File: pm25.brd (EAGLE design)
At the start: 47 x 33 mm, 12 parts, among them U2 CCS811B-JOPD500, U4 SI7021-A20-GM1R

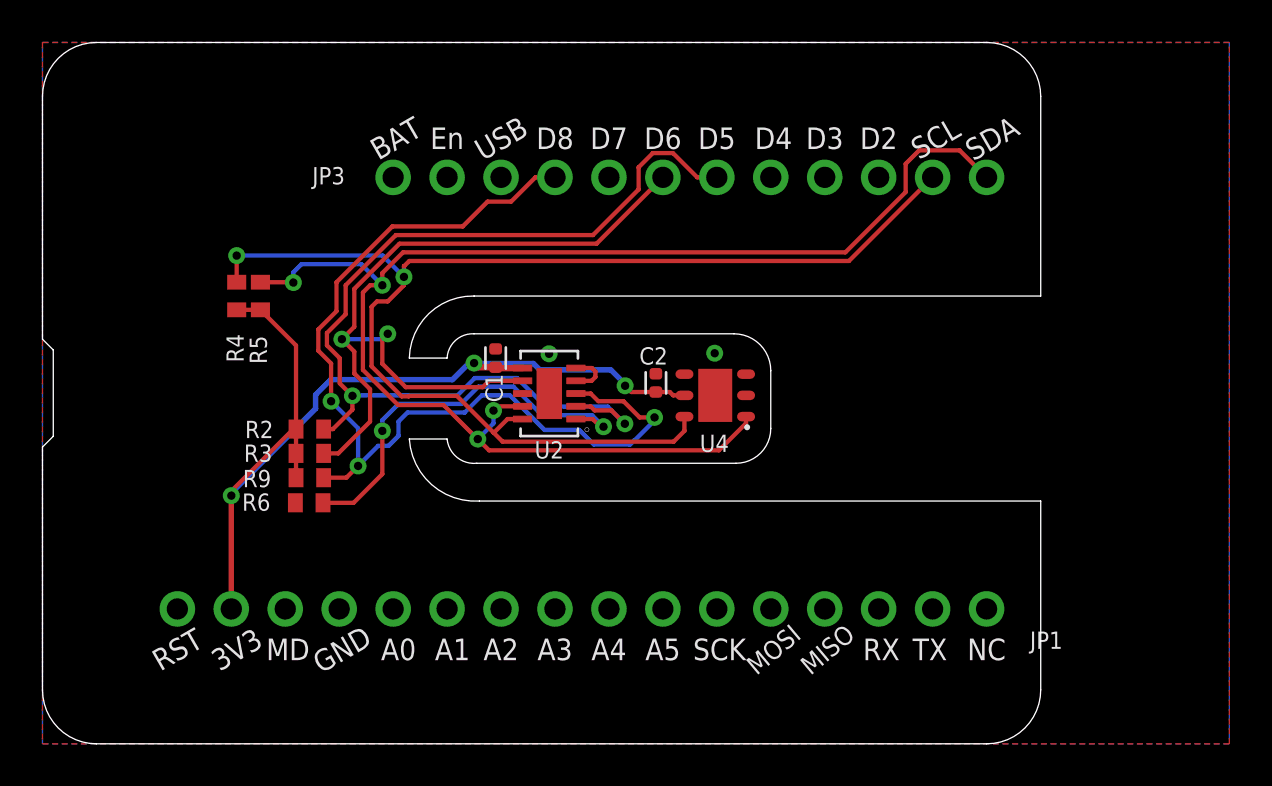
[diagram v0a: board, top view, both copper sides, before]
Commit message: Shrink width to 0.9" standard
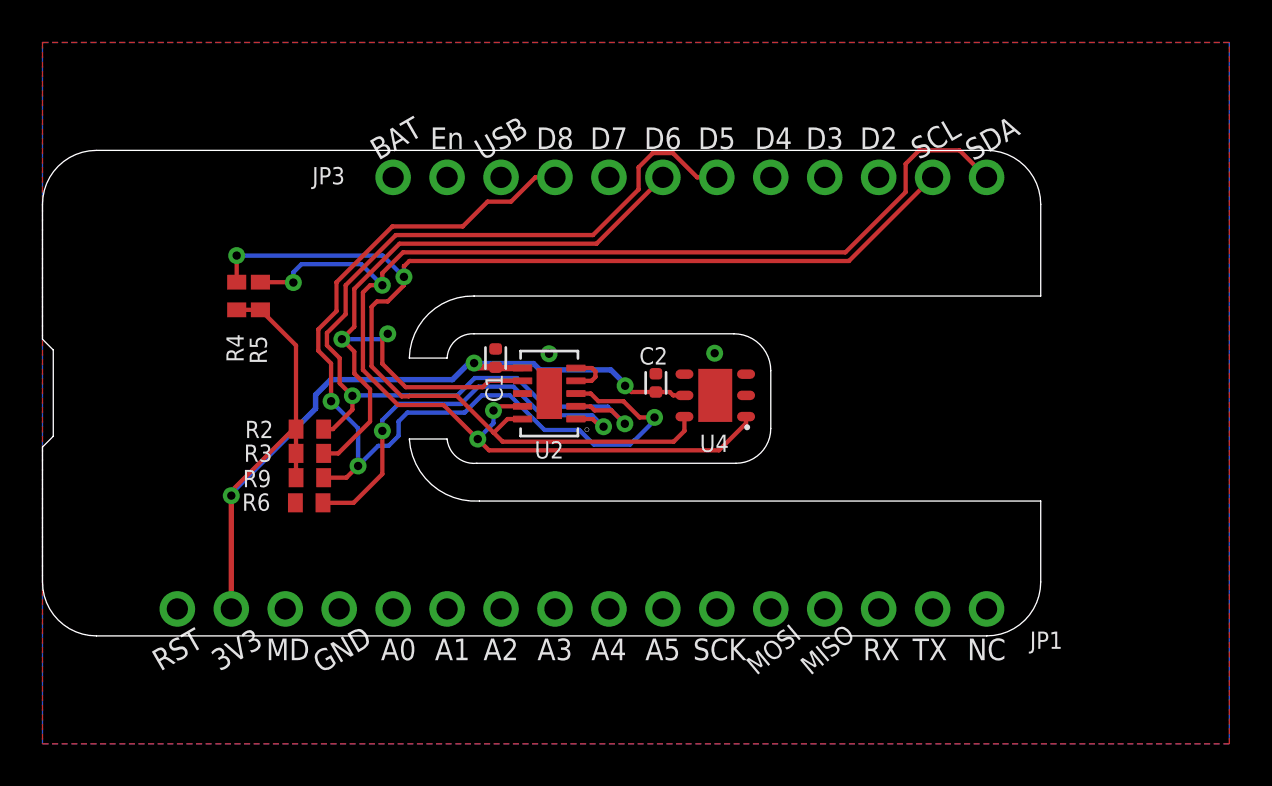
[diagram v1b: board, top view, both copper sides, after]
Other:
- board size 47 x 33 mm -> 47 x 22.9 mm
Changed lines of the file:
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@@
 <setting verticaltext="up"/>
 </settings>
-<grid distance="5" unitdist="mil" unit="mm" style="lines" multiple="1" display="no" altdistance="0.025" altunitdist="inch" altunit="mil"/>
+<grid distance="5" unitdist="mil" unit="inch" style="lines" multiple="1" display="no" altdistance="0.025" altunitdist="inch" altunit="mil"/>
 <layers>
-<layer number="1" name="Top" color="4" fill="1" visible="yes" active="yes"/>
+<layer number="1" name="Top" color="4" fill="1" visible="no" active="yes"/>
 <layer number="2" name="Route2" color="1" fill="3" visible="no" active="no"/>
 <layer number="3" name="Route3" color="4" fill="3" visible="no" active="no"/>
@@
 <layer number="14" name="Route14" color="1" fill="6" visible="no" active="no"/>
 <layer number="15" name="Route15" color="4" fill="6" visible="no" active="no"/>
-<layer number="16" name="Bottom" color="1" fill="1" visible="yes" active="yes"/>
-<layer number="17" name="Pads" color="2" fill="1" visible="yes" active="yes"/>
-<layer number="18" name="Vias" color="2" fill="1" visible="yes" active="yes"/>
-<layer number="19" name="Unrouted" color="6" fill="1" visible="yes" active="yes"/>
+<layer number="16" name="Bottom" color="1" fill="1" visible="no" active="yes"/>
+<layer number="17" name="Pads" color="2" fill="1" visible="no" active="yes"/>
+<layer number="18" name="Vias" color="2" fill="1" visible="no" active="yes"/>
+<layer number="19" name="Unrouted" color="6" fill="1" visible="no" active="yes"/>
 <layer number="20" name="Dimension" color="15" fill="1" visible="yes" active="yes"/>
-<layer number="21" name="tPlace" color="14" fill="1" visible="yes" active="yes"/>
-<layer number="22" name="bPlace" color="14" fill="1" visible="yes" active="yes"/>
-<layer number="23" name="tOrigins" color="14" fill="1" visible="yes" active="yes"/>
-<layer number="24" name="bOrigins" color="13" fill="1" visible="yes" active="yes"/>
-<layer number="25" name="tNames" color="7" fill="1" visible="yes" active="yes"/>
-<layer number="26" name="bNames" color="7" fill="1" visible="yes" active="yes"/>
+<layer number="21" name="tPlace" color="14" fill="1" visible="no" active="yes"/>
+<layer number="22" name="bPlace" color="14" fill="1" visible="no" active="yes"/>
+<layer number="23" name="tOrigins" color="14" fill="1" visible="no" active="yes"/>
+<layer number="24" name="bOrigins" color="13" fill="1" visible="no" active="yes"/>
+<layer number="25" name="tNames" color="7" fill="1" visible="no" active="yes"/>
+<layer number="26" name="bNames" color="7" fill="1" visible="no" active="yes"/>
 <layer number="27" name="tValues" color="7" fill="1" visible="no" active="yes"/>
 <layer number="28" name="bValues" color="7" fill="1" visible="no" active="yes"/>
@@
 <layer number="37" name="tTest" color="7" fill="1" visible="no" active="yes"/>
 <layer number="38" name="bTest" color="7" fill="1" visible="no" active="yes"/>
-<layer number="39" name="tKeepout" color="4" fill="11" visible="yes" active="yes"/>
-<layer number="40" name="bKeepout" color="1" fill="11" visible="yes" active="yes"/>
-<layer number="41" name="tRestrict" color="4" fill="10" visible="yes" active="yes"/>
-<layer number="42" name="bRestrict" color="1" fill="10" visible="yes" active="yes"/>
+<layer number="39" name="tKeepout" color="4" fill="11" visible="no" active="yes"/>
+<layer number="40" name="bKeepout" color="1" fill="11" visible="no" active="yes"/>
+<layer number="41" name="tRestrict" color="4" fill="10" visible="no" active="yes"/>
+<layer number="42" name="bRestrict" color="1" fill="10" visible="no" active="yes"/>
 <layer number="43" name="vRestrict" color="2" fill="10" visible="no" active="yes"/>
 <layer number="44" name="Drills" color="7" fill="1" visible="no" active="yes"/>
@@
 <layer number="49" name="Reference" color="7" fill="1" visible="no" active="yes"/>
 <layer number="50" name="dxf" color="7" fill="1" visible="no" active="no"/>
-<layer number="51" name="tDocu" color="7" fill="1" visible="yes" active="yes"/>
-<layer number="52" name="bDocu" color="7" fill="1" visible="yes" active="yes"/>
+<layer number="51" name="tDocu" color="7" fill="1" visible="no" active="yes"/>
+<layer number="52" name="bDocu" color="7" fill="1" visible="no" active="yes"/>
 <layer number="53" name="tGND_GNDA" color="7" fill="9" visible="no" active="no"/>
 <layer number="54" name="bGND_GNDA" color="1" fill="9" visible="no" active="no"/>
@@
 <fusionsync huburn="a.cGVyc29uYWw6dWUyZDcxOWFm" projecturn="a.cGVyc29uYWw6dWUyZDcxOWFmIzIwMTkwMzIxMTgzNjY2NTgx" f3durn="urn:adsk.wipprod:dm.lineage:of-WC7iUTR6j-QJaXZ4WSA" pcbguid="2ada34ed-02e3-4764-ae65-c304e2d58fe2" lastpulledtime="" lastsyncedchangeguid="c324f360-4e1b-41e3-ea26-84c460706219"/>
 <plain>
-<wire x1="2.54" y1="0" x2="44.46" y2="0" width="0" layer="20"/>
-<wire x1="44.46" y1="0" x2="47" y2="2.54" width="0" layer="20" curve="90"/>
-<wire x1="47" y1="2.54" x2="47" y2="11.43" width="0" layer="20"/>
-<wire x1="47" y1="21.082" x2="47" y2="30.48" width="0" layer="20"/>
-<wire x1="47" y1="30.48" x2="44.46" y2="33.02" width="0" layer="20" curve="90"/>
-<wire x1="44.46" y1="33.02" x2="2.54" y2="33.02" width="0" layer="20"/>
-<wire x1="2.54" y1="33.02" x2="0" y2="30.48" width="0" layer="20" curve="90"/>
-<wire x1="0" y1="30.48" x2="0" y2="19.05" width="0" layer="20"/>
+<wire x1="2.54" y1="5.08" x2="44.46" y2="5.08" width="0" layer="20"/>
+<wire x1="44.46" y1="5.08" x2="47" y2="7.62" width="0" layer="20" curve="90"/>
+<wire x1="47" y1="7.62" x2="47" y2="11.43" width="0" layer="20"/>
+<wire x1="47" y1="21.082" x2="47" y2="25.4" width="0" layer="20"/>
+<wire x1="47" y1="25.4" x2="44.46" y2="27.94" width="0" layer="20" curve="90"/>
+<wire x1="44.46" y1="27.94" x2="2.54" y2="27.94" width="0" layer="20"/>
+<wire x1="2.54" y1="27.94" x2="0" y2="25.4" width="0" layer="20" curve="90"/>
+<wire x1="0" y1="25.4" x2="0" y2="19.05" width="0" layer="20"/>
 <wire x1="0" y1="19.05" x2="0.508" y2="18.542" width="0" layer="20"/>
 <wire x1="0.508" y1="18.542" x2="0.508" y2="14.478" width="0" layer="20"/>
 <wire x1="0.508" y1="14.478" x2="0" y2="13.97" width="0" layer="20"/>
-<wire x1="0" y1="13.97" x2="0" y2="2.54" width="0" layer="20"/>
-<wire x1="0" y1="2.54" x2="2.54" y2="0" width="0" layer="20" curve="90"/>
+<wire x1="0" y1="13.97" x2="0" y2="7.62" width="0" layer="20"/>
+<wire x1="0" y1="7.62" x2="2.54" y2="5.08" width="0" layer="20" curve="90"/>
 <text x="21.59" y="24.257" size="1.016" layer="22" ratio="12" rot="SMR270" align="center">USB</text>
 <text x="41.9354" y="23.9522" size="1.016" layer="22" ratio="12" rot="MR90" align="center">SCL</text>
